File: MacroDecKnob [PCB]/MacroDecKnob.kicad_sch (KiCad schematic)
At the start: 36 parts, among them J1 Batt, J2 Mounting Hole, J3 Mounting Hole, J4 Mounting Hole, J5 Mounting Hole, J6 Mounting Hole, J7 5V-ARGB, SW1 SW_Push, SW10 SW_Push, SW11 SW_Push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

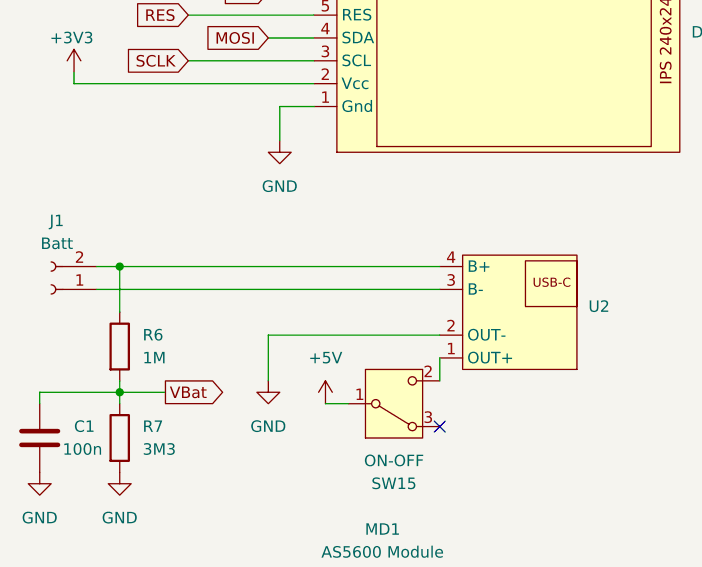
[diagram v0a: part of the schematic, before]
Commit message: upgrade 2"display
display 320x 240 upgrade
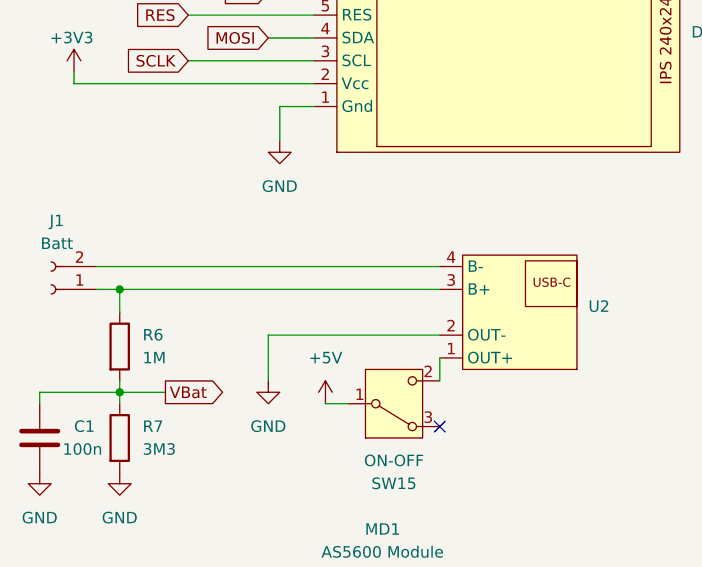
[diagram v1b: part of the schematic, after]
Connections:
- net at J1.1 (Pin_1), U2.3 (B+): now also R6.1
- net at J1.2 (Pin_2), U2.4 (B-): no longer R6.1
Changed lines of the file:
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@@
+	)
+	(junction
+		(at 25.4 139.7)
+		(diameter 0)
+		(color 0 0 0 0)
 	)
 	(junction
@@
 	)
 	(junction
-		(at 25.4 137.16)
-		(diameter 0)
-		(color 0 0 0 0)
-	)
-	(junction
 		(at 111.76 123.19)
 		(diameter 0)
@@
 	(wire
 		(pts
-			(xy 25.4 137.16) (xy 25.4 142.24)
+			(xy 25.4 139.7) (xy 25.4 142.24)
+		)
+		(stroke
+			(width 0)
+			(type default)
+		)
+	)
+	(wire
+		(pts
+			(xy 25.4 139.7) (xy 60.96 139.7)
 		)
 		(stroke
@@
 	(wire
 		(pts
-			(xy 25.4 137.16) (xy 60.96 137.16)
+			(xy 22.86 137.16) (xy 60.96 137.16)
 		)
 		(stroke
@@
 	(wire
 		(pts
-			(xy 22.86 137.16) (xy 25.4 137.16)
-		)
-		(stroke
-			(width 0)
-			(type default)
-		)
-	)
-	(wire
-		(pts
 			(xy 120.65 82.55) (xy 127 82.55)
 		)
@@
 	(wire
 		(pts
-			(xy 22.86 139.7) (xy 60.96 139.7)
-		)
-		(stroke
+			(xy 22.86 139.7) (xy 25.4 139.7)
+		)
+		(stroke
